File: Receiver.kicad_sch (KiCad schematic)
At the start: 27 parts, among them J15 UFL, U19 TPRT9013-33, U20 SX1280IMLTRT, U21 AT2401C, Y2 52MHz/10ppm

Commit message: Connectors and tag
Added bulk capacitance for each ESC.
Added SWD connector.
Updated all tags.

TODO:
Add pads for the unconnected GPIO pins.
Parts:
- renumbered C75 to C100, C61 to C86, C62 to C87, C63 to C88, C64 to C89, C65 to C90, C66 to C91, C67 to C92, C68 to C93, C69 to C94, C70 to C95, C71 to C96, C72 to C97, C73 to C98, C74 to C99, R86 to R85, R87 to R86, R88 to R87

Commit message: Missing labels and revision
First complete revision of the schematic.
Added missing labels.

TODO:
Continue reviewing the schematic.
Include net coloring.
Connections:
- net VR_PA: now reaches C88.1, U20.1 (VR_PA)
- net DCC_SW: now reaches L3.1, U20.14 (DCC_SW)
- net XTA: now reaches U20.4 (XTA), Y2.3
- net XTB: now reaches U20.6 (XTB), Y2.1
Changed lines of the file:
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@@
+	)
+	(junction
+		(at 81.28 35.56)
+		(diameter 0)
+		(color 0 0 0 0)
 	)
 	(junction
@@
 	)
 	(junction
-		(at 81.28 35.56)
-		(diameter 0)
-		(color 0 0 0 0)
-	)
-	(junction
 		(at 213.36 135.89)
 		(diameter 0)
@@
 	)
 	(junction
-		(at 160.02 57.15)
-		(diameter 0)
-		(color 0 0 0 0)
-	)
-	(junction
 		(at 95.25 132.08)
 		(diameter 0)
@@
 	(wire
 		(pts
+			(xy 78.74 35.56) (xy 81.28 35.56)
+		)
+		(stroke
+			(width 0)
+			(type default)
+		)
+	)
+	(wire
+		(pts
 			(xy 80.01 73.66) (xy 82.55 73.66)
 		)
@@
 	(wire
 		(pts
-			(xy 78.74 35.56) (xy 81.28 35.56)
-		)
-		(stroke
-			(width 0)
-			(type default)
-		)
-	)
-	(wire
-		(pts
 			(xy 217.17 85.09) (xy 217.17 87.63)
 		)
@@
 	(wire
 		(pts
-			(xy 99.06 38.1) (xy 88.9 38.1)
-		)
-		(stroke
-			(width 0)
-			(type default)
-		)
-	)
-	(wire
-		(pts
 			(xy 193.04 66.04) (xy 207.01 66.04)
 		)
@@
 	(wire
 		(pts
-			(xy 160.02 57.15) (xy 162.56 57.15)
-		)
-		(stroke
-			(width 0)
-			(type default)
-		)
-	)
-	(wire
-		(pts
 			(xy 232.41 45.72) (xy 232.41 43.18)
 		)
@@
 	(wire
 		(pts
+			(xy 81.28 35.56) (xy 111.76 35.56)
+		)
+		(stroke
+			(width 0)
+			(type default)
+		)
+	)
+	(wire
+		(pts
 			(xy 217.17 82.55) (xy 217.17 85.09)
 		)
@@
 	(wire
 		(pts
+			(xy 88.9 38.1) (xy 99.06 38.1)
+		)
+		(stroke
+			(width 0)
+			(type default)
+		)
+	)
+	(wire
+		(pts
 			(xy 81.28 48.26) (xy 81.28 50.8)
 		)
@@
 		(pts
 			(xy 95.25 129.54) (xy 95.25 132.08)
-		)
-		(stroke
-			(width 0)
-			(type default)
-		)
-	)
-	(wire
-		(pts
-			(xy 81.28 35.56) (xy 111.76 35.56)
 		)
 		(stroke
@@
 		)
 	)
+	(label "DCC_SW"
+		(at 134.665 59.69 0)
+		(effects
+			(font
+				(size 1.27 1.27)
+			)
+			(justify left bottom)
+		)
+	)
 	(label "RFIO"
 		(at 204.47 73.66 180)
@@
 		)
 	)
+	(label "XTA"
+		(at 99.06 67.31 180)
+		(effects
+			(font
+				(size 1.27 1.27)
+			)
+			(justify right bottom)
+		)
+	)
 	(label "RFIO"
 		(at 185.42 135.89 180)
@@
 	)
 	(label "DCC_FB"
-		(at 162.56 57.15 0)
+		(at 134.62 57.15 0)
 		(effects
 			(font
@@
 		)
 	)
+	(label "XTB"
+		(at 99.06 69.85 180)
+		(effects
+			(font
+				(size 1.27 1.27)
+			)
+			(justify right bottom)
+		)
+	)
 	(label "ANT_FILT"
 		(at 130.81 133.35 180)
 		(effects
 			(font
+				(size 1.27 1.27)
+			)
+			(justify right bottom)
+		)
+	)
+	(label "VR_PA"
+		(at 97.79 38.1 180)
+		(effects
+			(font

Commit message: ESC layout and footprints
Added the initial ESC layout.
Updated some footprints for compatibility.
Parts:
- U20: footprint Package_DFN_QFN:QFN-24-1EP_4x4mm_P0.5mm_EP2.6x2.6mm_ThermalVias -> Custom_Parts:QFN-24_4x4mm_P0.5mm_EP
- U21: footprint Package_DFN_QFN:QFN-16-1EP_3x3mm_P0.5mm_EP1.7x1.7mm_ThermalVias -> Custom_Parts:QFN-16_3x3mm_P0.5mm_EP1.7x1.7mm_EP
- renumbered C96 to C100, C97 to C101, C98 to C102, C99 to C103, C100 to C104, C86 to C90, C87 to C91, C88 to C92, C89 to C93, C90 to C94, C91 to C95, C92 to C96, C93 to C97, C94 to C98, C95 to C99
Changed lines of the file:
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@@
 		(on_board yes)
 		(dnp no)
-		(property "Reference" "C90"
+		(property "Reference" "C94"
 			(at 140.208 40.64 0)
 			(effects
@@
 			(project "ThunderHorse"
 				(path "/ac187c6c-fa53-41cc-bce1-6f39a42a92e8/bc3cf81e-9940-4196-8a64-4d021e41ea8d"
-					(reference "C90")
+					(reference "C94")
 					(unit 1)
 				)
@@
 		(dnp no)
 		(fields_autoplaced yes)
-		(property "Reference" "C89"
+		(property "Reference" "C93"
 			(at 99.06 139.6999 0)
 			(effects
@@
 			(project "ThunderHorse"
 				(path "/ac187c6c-fa53-41cc-bce1-6f39a42a92e8/bc3cf81e-9940-4196-8a64-4d021e41ea8d"
-					(reference "C89")
+					(reference "C93")
 					(unit 1)
 				)
@@
 		(dnp no)
 		(fields_autoplaced yes)
-		(property "Reference" "C91"
+		(property "Reference" "C95"
 			(at 160.02 40.6399 0)
 			(effects
@@
 			(project "ThunderHorse"
 				(path "/ac187c6c-fa53-41cc-bce1-6f39a42a92e8/bc3cf81e-9940-4196-8a64-4d021e41ea8d"
-					(reference "C91")
+					(reference "C95")
 					(unit 1)
 				)
@@
 		(dnp no)
 		(fields_autoplaced yes)
-		(property "Reference" "C86"
+		(property "Reference" "C90"
 			(at 73.66 139.6999 0)
 			(effects
@@
 			(project "ThunderHorse"
 				(path "/ac187c6c-fa53-41cc-bce1-6f39a42a92e8/bc3cf81e-9940-4196-8a64-4d021e41ea8d"
-					(reference "C86")
+					(reference "C90")
 					(unit 1)
 				)
@@
 		(dnp yes)
 		(fields_autoplaced yes)
-		(property "Reference" "C98"
+		(property "Reference" "C102"
 			(at 217.17 140.9699 0)
 			(effects
@@
 			(project "ThunderHorse"
 				(path "/ac187c6c-fa53-41cc-bce1-6f39a42a92e8/bc3cf81e-9940-4196-8a64-4d021e41ea8d"
-					(reference "C98")
+					(reference "C102")
 					(unit 1)
 				)
@@
 		(dnp yes)
 		(fields_autoplaced yes)
-		(property "Reference" "C95"
+		(property "Reference" "C99"
 			(at 204.47 140.9699 0)
 			(effects
@@
 			(project "ThunderHorse"
 				(path "/ac187c6c-fa53-41cc-bce1-6f39a42a92e8/bc3cf81e-9940-4196-8a64-4d021e41ea8d"
-					(reference "C95")
+					(reference "C99")
 					(unit 1)
 				)
@@
 		(dnp no)
 		(fields_autoplaced yes)
-		(property "Reference" "C88"
+		(property "Reference" "C92"
 			(at 92.71 43.1799 0)
 			(effects
@@
 			(project "ThunderHorse"
 				(path "/ac187c6c-fa53-41cc-bce1-6f39a42a92e8/bc3cf81e-9940-4196-8a64-4d021e41ea8d"
-					(reference "C88")
+					(reference "C92")
 					(unit 1)
 				)
@@
 		(on_board yes)
 		(dnp no)
-		(property "Reference" "C87"
+		(property "Reference" "C91"
 			(at 73.914 43.18 0)
 			(effects
@@
 			(project "ThunderHorse"
 				(path "/ac187c6c-fa53-41cc-bce1-6f39a42a92e8/bc3cf81e-9940-4196-8a64-4d021e41ea8d"
-					(reference "C87")
+					(reference "C91")
 					(unit 1)
 				)
@@
 		(dnp yes)
 		(fields_autoplaced yes)
-		(property "Reference" "C93"
+		(property "Reference" "C97"
 			(at 191.77 140.9699 0)
 			(effects
@@
 			(project "ThunderHorse"
 				(path "/ac187c6c-fa53-41cc-bce1-6f39a42a92e8/bc3cf81e-9940-4196-8a64-4d021e41ea8d"
-					(reference "C93")
+					(reference "C97")
 					(unit 1)
 				)
@@
 		(dnp no)
 		(fields_autoplaced yes)
-		(property "Reference" "C100"
+		(property "Reference" "C104"
 			(at 236.22 48.2599 0)
 			(effects
@@
 			(project "ThunderHorse"
 				(path "/ac187c6c-fa53-41cc-bce1-6f39a42a92e8/bc3cf81e-9940-4196-8a64-4d021e41ea8d"
-					(reference "C100")
+					(reference "C104")
 					(unit 1)
 				)
@@
 		(dnp no)
 		(fields_autoplaced yes)
-		(property "Reference" "C96"
+		(property "Reference" "C100"
 			(at 208.28 48.2599 0)
 			(effects
@@
 			(project "ThunderHorse"
 				(path "/ac187c6c-fa53-41cc-bce1-6f39a42a92e8/bc3cf81e-9940-4196-8a64-4d021e41ea8d"
-					(reference "C96")
+					(reference "C100")
 					(unit 1)
 				)
@@
 		(dnp yes)
 		(fields_autoplaced yes)
-		(property "Reference" "C99"
+		(property "Reference" "C103"
 			(at 219.71 128.27 90)
 			(effects
@@
 			(project "ThunderHorse"
 				(path "/ac187c6c-fa53-41cc-bce1-6f39a42a92e8/bc3cf81e-9940-4196-8a64-4d021e41ea8d"
-					(reference "C99")
+					(reference "C103")
 					(unit 1)
 				)
@@
 		(dnp no)
 		(fields_autoplaced yes)
-		(property "Reference" "C92"
+		(property "Reference" "C96"
 			(at 163.83 62.2299 0)
 			(effects
@@
 			(project "ThunderHorse"
 				(path "/ac187c6c-fa53-41cc-bce1-6f39a42a92e8/bc3cf81e-9940-4196-8a64-4d021e41ea8d"
-					(reference "C92")
+					(reference "C96")
 					(unit 1)
 				)
@@
 			)
 		)
-		(property "Footprint" "Package_DFN_QFN:QFN-24-1EP_4x4mm_P0.5mm_EP2.6x2.6mm_ThermalVias"
+		(property "Footprint" "Custom_Parts:QFN-24_4x4mm_P0.5mm_EP"
 			(at 130.81 145.72 0)
 			(effects
@@
 		(dnp yes)
 		(fields_autoplaced yes)
-		(property "Reference" "C97"
+		(property "Reference" "C101"
 			(at 207.01 119.38 90)
 			(effects
@@
 			(project "ThunderHorse"
 				(path "/ac187c6c-fa53-41cc-bce1-6f39a42a92e8/bc3cf81e-9940-4196-8a64-4d021e41ea8d"
-					(reference "C97")
+					(reference "C101")
 					(unit 1)
 				)
@@
 			)
 		)
-		(property "Footprint" "Package_DFN_QFN:QFN-16-1EP_3x3mm_P0.5mm_EP1.7x1.7mm_ThermalVias"
+		(property "Footprint" "Custom_Parts:QFN-16_3x3mm_P0.5mm_EP1.7x1.7mm_EP"
 			(at 180.848 95.25 0)
 			(effects
@@
 		(on_board yes)
 		(dnp no)
-		(property "Reference" "C94"
+		(property "Reference" "C98"
 			(at 189.992 48.26 0)
 			(effects
@@
 			(project "ThunderHorse"
 				(path "/ac187c6c-fa53-41cc-bce1-6f39a42a92e8/bc3cf81e-9940-4196-8a64-4d021e41ea8d"
-					(reference "C94")
+					(reference "C98")
 					(unit 1)
 				)

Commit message: Initial layout
Completed an initial layout of the main components.

TODO
Route the ESCs and check the result.
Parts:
- renumbered C99 to C100, C100 to C101, C101 to C102, C102 to C103, C103 to C104, C104 to C105, C90 to C91, C91 to C92, C92 to C93, C93 to C94, C94 to C95, C95 to C96, C96 to C97, C97 to C98, C98 to C99, U19 to U20, U20 to U21, U21 to U22

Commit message: MCU layout
Updated the schematic labels.
Continued the MCU layout.
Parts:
- renumbered R85 to R87, R86 to R88, R87 to R89

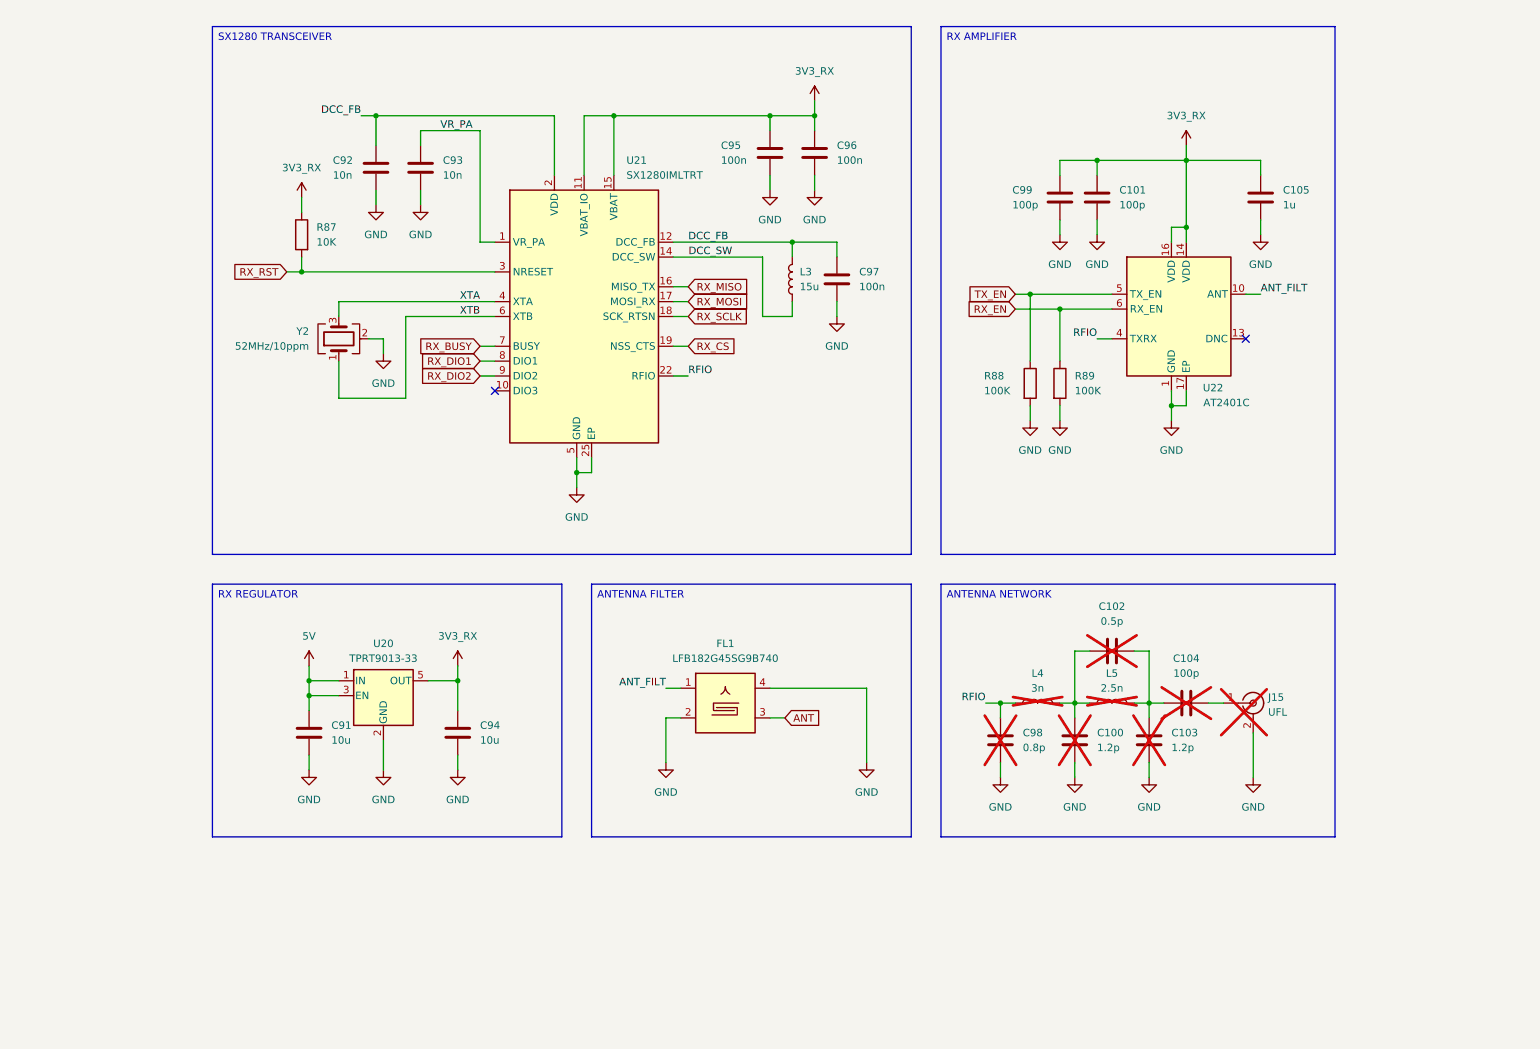
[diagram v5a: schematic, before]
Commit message: Schematic revision
Added an ESP32 C3 for the ELRS receiver.
Updated the protection approach for the board.
Updated the net nodes.
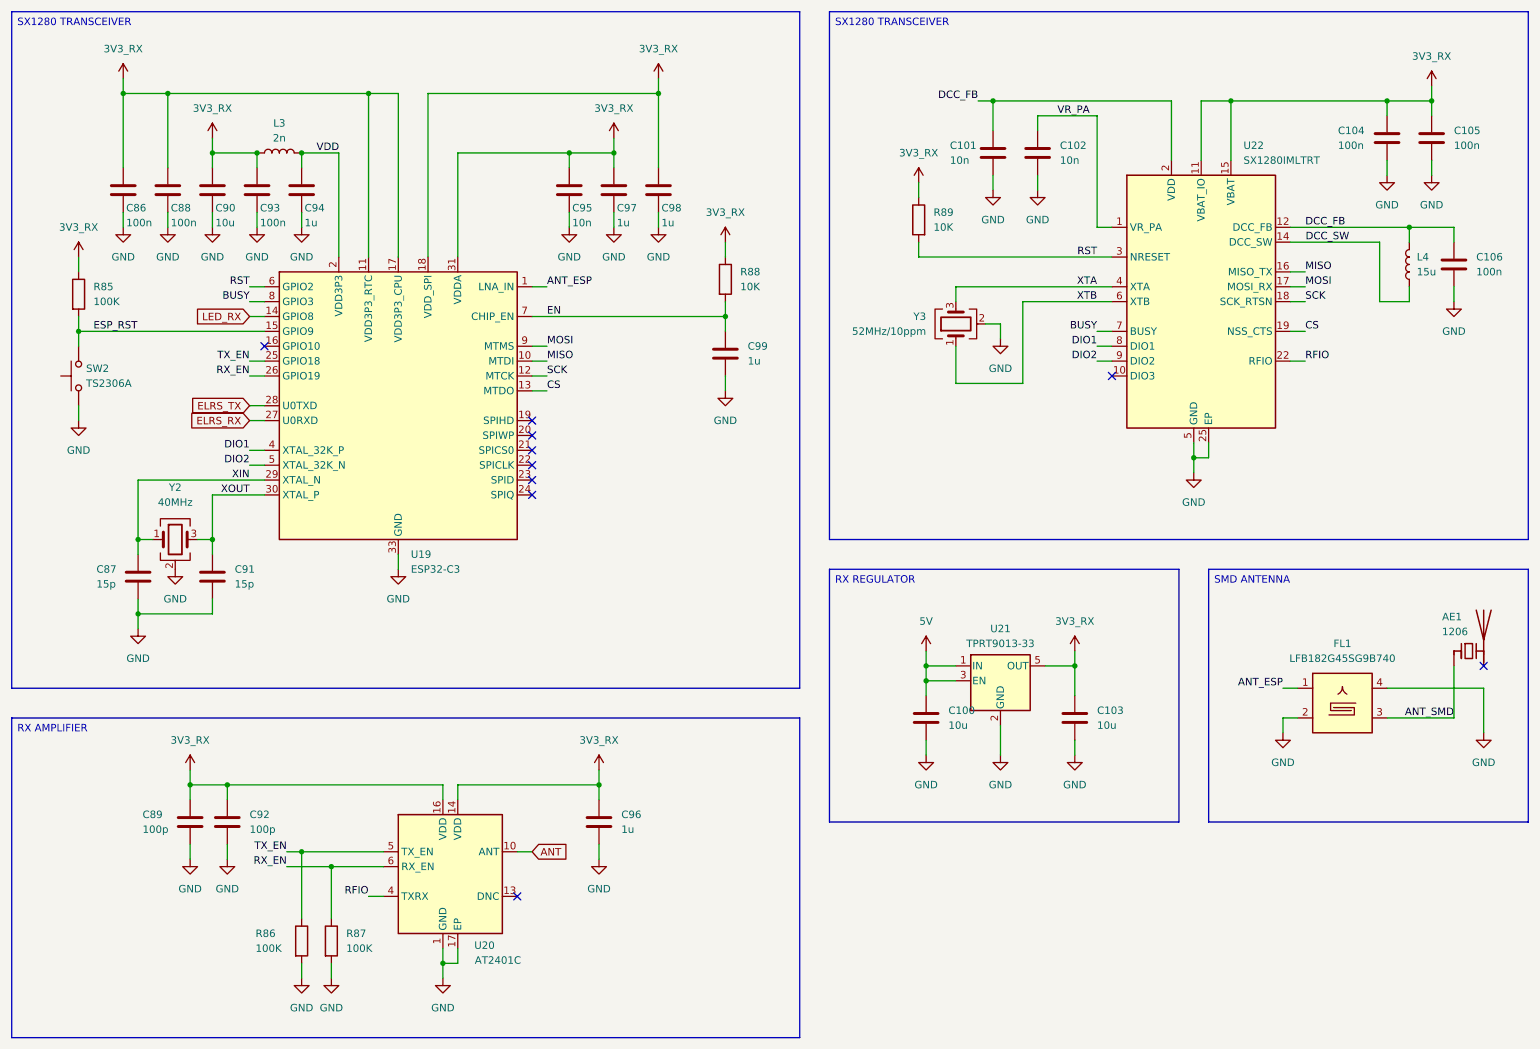
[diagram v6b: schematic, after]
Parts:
- removed C100, C103: 1.2p, symbol Device:C
- removed C102: 0.5p, symbol Device:C
- removed C104: 100p, symbol Device:C
- removed J15: UFL, Connector_Coaxial:U.FL_Hirose_U.FL-R-SMT-1_Vertical, symbol Connector:Conn_Coaxial
- removed L4: 3n, symbol Device:L
- removed L5: 2.5n, symbol Device:L
- added AE1: 1206, Inductor_SMD:L_1206_3216Metric, symbol Device:Antenna_Chip
- added C86, C88, C93: 100n, Capacitor_SMD:C_0603_1608Metric, symbol Device:C
- added C87, C91: 15p, Capacitor_SMD:C_0603_1608Metric, symbol Device:C
- added C90: 10u, Capacitor_SMD:C_0805_2012Metric, symbol Device:C
- added C94, C97, C99: 1u, Capacitor_SMD:C_0603_1608Metric, symbol Device:C
- added C95: 10n, Capacitor_SMD:C_0603_1608Metric, symbol Device:C
- added L3: 2n, Inductor_SMD:L_0603_1608Metric, symbol Device:L
- added R85: 100K, Resistor_SMD:R_0603_1608Metric, symbol Device:R
- added R88: 10K, Resistor_SMD:R_0603_1608Metric, symbol Device:R
- added SW2: TS2306A, Custom_Parts:SW_SMD_3.0x2.0_PUSH, symbol Switch:SW_Push
- added U19: ESP32-C3, Package_DFN_QFN:QFN-32-1EP_5x5mm_P0.5mm_EP3.7x3.7mm, symbol Custom_Parts:ESP32-C3
- added Y2: 40MHz, Crystal:Crystal_SMD_2016-4Pin_2.0x1.6mm, symbol Device:Crystal_GND24
- C98: value 0.8p -> 1u; footprint (none) -> Capacitor_SMD:C_0603_1608Metric; now fitted; now in the parts list
- renumbered C91 to C100, C92 to C101, C93 to C102, C94 to C103, C95 to C104, C96 to C105, C97 to C106, C99 to C89, C101 to C92, C105 to C96, L3 to L4, R88 to R86, R89 to R87, R87 to R89, U22 to U20, U20 to U21, U21 to U22, Y2 to Y3
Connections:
- net 3V3_RX: now also C98.1, C86.1, C88.1, C90.1, C93.1, C95.1, C97.1, L3.1, R85.1, R88.1, U19.11 (VDD3P3_RTC), U19.17 (VDD3P3_CPU), U19.18 (VDD_SPI), U19.31 (VDDA), U19.32 (VDDA)
- net ANT: now also U20.10 (ANT); no longer FL1.3
- net GND: now also C86.2, C87.2, C88.2, C90.2, C91.2, C93.2, C94.2, C95.2, C97.2, C99.2, SW2.1, U19.33 (GND), Y2.2 (G), Y2.4 (G)
- net RFIO: no longer C98.1
- net RX_EN: now also U19.26 (GPIO19)
- net TX_EN: now also U19.25 (GPIO18)
- net ANT_FILT renamed ANT_ESP
- net ANT_ESP: now also U19.1 (LNA_IN); no longer U20.10 (ANT)
- net RX_BUSY renamed BUSY
- net BUSY: now also U19.8 (GPIO3)
- net RX_CS renamed CS
- net CS: now also U19.13 (MTDO)
- net RX_DIO1 renamed DIO1
- net DIO1: now also U19.4 (XTAL_32K_P)
- net RX_DIO2 renamed DIO2
- net DIO2: now also U19.5 (XTAL_32K_N)
- net RX_MISO renamed MISO
- net MISO: now also U19.10 (MTDI)
- net RX_MOSI renamed MOSI
- net MOSI: now also U19.9 (MTMS)
- net RX_RST renamed RST
- net RST: now also U19.6 (GPIO2)
- net RX_SCLK renamed SCK
- net SCK: now also U19.12 (MTCK)
- new net ANT_SMD: AE1.1 (FEED), FL1.3
- new net ELRS_RX: U19.27 (U0RXD)
- new net ELRS_TX: U19.28 (U0TXD)
- new net EN: C99.1, R88.2, U19.7 (CHIP_EN)
- new net ESP_RST: R85.2, SW2.2, U19.15 (GPIO9)
- new net LED_RX: U19.14 (GPIO8)
- new net VDD: C94.1, L3.2, U19.2 (VDD3P3), U19.3 (VDD3P3)
- new net XIN: C87.1, U19.29 (XTAL_N), Y2.1
- new net XOUT: C91.1, U19.30 (XTAL_P), Y2.3
- no-connect marks 2 -> 10
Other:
- moved on the sheet: C100, C101, C102, C103, C104, C105, C106, C89, C92, C96, L4, R86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

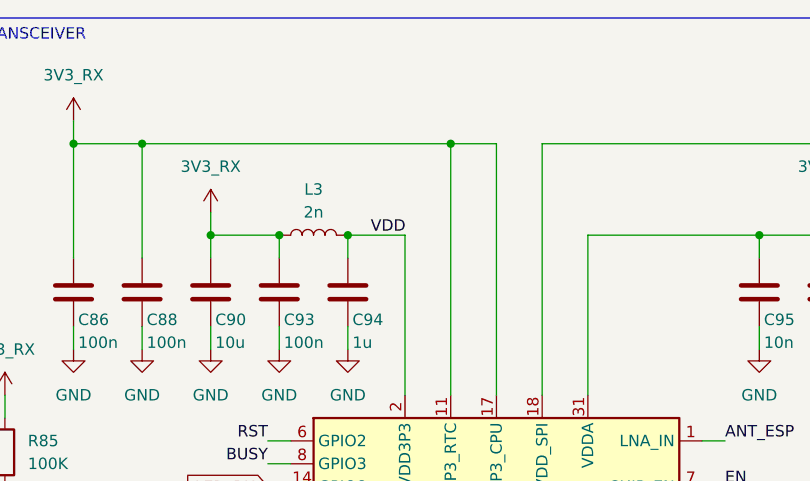
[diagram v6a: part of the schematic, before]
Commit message: Schematic and PCB
Reviewed the schematic and deleted unused components.
Updated the PCB and also removed unused footprints.
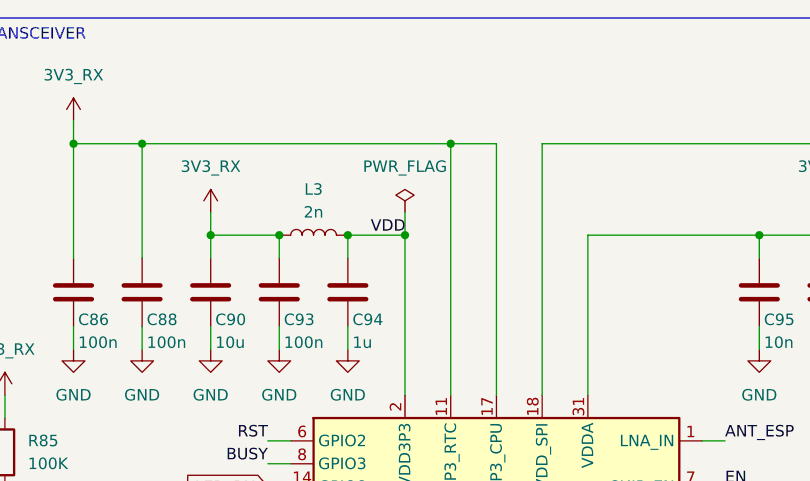
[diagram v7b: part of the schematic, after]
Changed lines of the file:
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@@
 	)
 	(junction
+		(at 74.93 41.91)
+		(diameter 0)
+		(color 0 0 0 0)
+	)
+	(junction
 		(at 40.64 120.65)
 		(diameter 0)
@@
 	(wire
 		(pts
+			(xy 74.93 39.37) (xy 74.93 41.91)
+		)
+		(stroke
+			(width 0)
+			(type default)
+		)
+	)
+	(wire
+		(pts
 			(xy 227.33 33.02) (xy 222.25 33.02)
 		)
@@
 					(unit 1)
 				)
+			)
+		)
+	)
+	(symbol
+		(lib_id "power:PWR_FLAG")
+		(at 74.93 39.37 0)
+		(unit 1)
+		(exclude_from_sim no)
+		(in_bom yes)
+		(on_board yes)
+		(dnp no)
+		(fields_autoplaced yes)
+		(property "Reference" "#FLG09"
+			(at 74.93 37.465 0)
+			(effects
+				(font
+					(size 1.27 1.27)
+				)
+				(hide yes)
+			)
+		)
+		(property "Value" "PWR_FLAG"
+			(at 74.93 34.29 0)
+			(effects
+				(font
+					(size 1.27 1.27)
+				)
+			)
+		)
+		(property "Footprint" ""
+			(at 74.93 39.37 0)
+			(effects
+				(font
+					(size 1.27 1.27)
+				)
+				(hide yes)
+			)
+		)
+		(property "Datasheet" "~"
+			(at 74.93 39.37 0)
+			(effects
+				(font
+					(size 1.27 1.27)
+				)
+				(hide yes)
+			)
+		)
+		(property "Description" "Special symbol for telling ERC where power comes from"
+			(at 74.93 39.37 0)
+			(effects
+				(font
+					(size 1.27 1.27)
+				)
+				(hide yes)
+			)
+		)
+		(pin "1"
+		)
+		(instances
+			(project "ThunderHorse"
+				(path "/ac187c6c-fa53-41cc-bce1-6f39a42a92e8/bc3cf81e-9940-4196-8a64-4d021e41ea8d"
+					(reference "#FLG09")
+					(unit 1)
+				)
